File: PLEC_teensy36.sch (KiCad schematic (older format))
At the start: 4 parts, among them U8 Teensy3.6

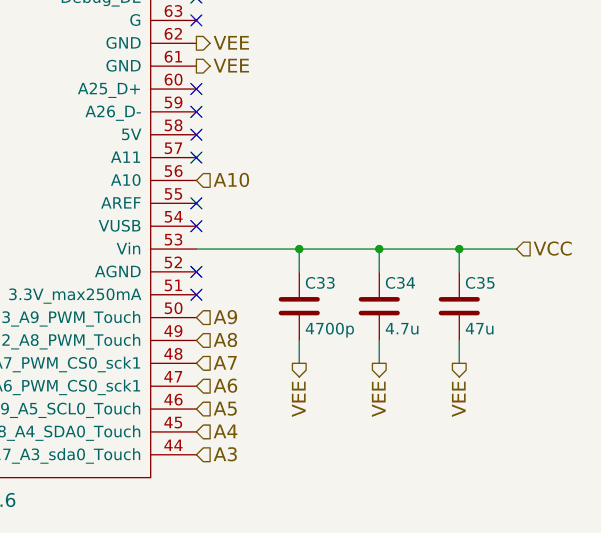
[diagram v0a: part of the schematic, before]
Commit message: Almost done with layout; need to rearrange uC pins
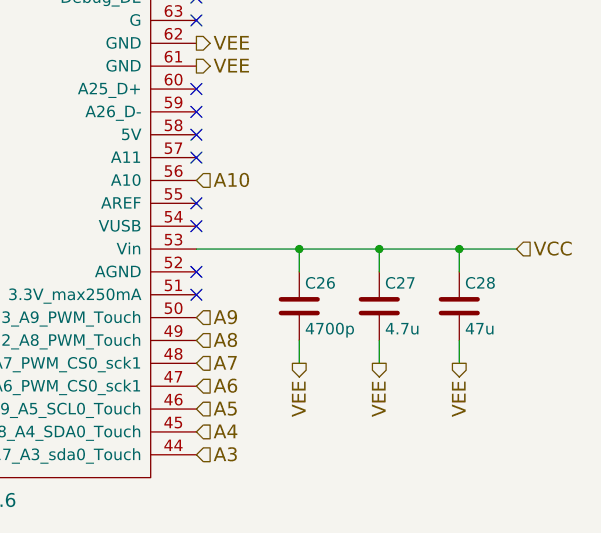
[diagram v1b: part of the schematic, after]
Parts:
- renumbered C33 to C26, C34 to C27, C35 to C28
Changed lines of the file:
@@
 NoConn ~ 6650 4600
 $Comp
-L C C34
+L C C27
 U 1 1 5A7ABA8B
 P 7450 5450
-F 0 "C34" H 7475 5550 50  0000 L CNN
+F 0 "C27" H 7475 5550 50  0000 L CNN
 F 1 "4.7u" H 7475 5350 50  0000 L CNN
 F 2 "PLEC:THTm_1.5Px4Dx7H_4.7u" H 7488 5300 50  0001 C CNN
@@
 $EndComp
 $Comp
-L C C33
+L C C26
 U 1 1 5A7ABABC
 P 7100 5450
-F 0 "C33" H 7125 5550 50  0000 L CNN
+F 0 "C26" H 7125 5550 50  0000 L CNN
 F 1 "4700p" H 7125 5350 50  0000 L CNN
 F 2 "PLEC:THTt_100Px150Lx100Wx183H_4700p" H 7138 5300 50  0001 C CNN
@@
 NoConn ~ 6650 5000
 $Comp
-L C C35
+L C C28
 U 1 1 5A75E6B2
 P 7800 5450
-F 0 "C35" H 7825 5550 50  0000 L CNN
+F 0 "C28" H 7825 5550 50  0000 L CNN
 F 1 "47u" H 7825 5350 50  0000 L CNN
 F 2 "PLEC:THTm_2Px4Dx12H_47u" H 7838 5300 50  0001 C CNN

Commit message: Finished PCB with no errors
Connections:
- net A0: now also U8.30 (33_A14_CAN1TX_scl0); no longer U8.41 (14_A0_PWM_sck0)
- net A1: now also U8.31 (34_A15_CAN1TX_sda0); no longer U8.42 (15_A1_CS0_Touch)
- net A10: now also U8.43 (16_A2_scl0_Touch); no longer U8.56 (A10)
- net A11: now also U8.44 (17_A3_sda0_Touch); no longer U8.38 (A22_DAC1)
- net A12: now also U8.41 (14_A0_PWM_sck0); no longer U8.79 (50_A24)
- net A13: now also U8.42 (15_A1_CS0_Touch); no longer U8.78 (49_A23)
- net A2: now also U8.32 (35_A16_PWM); no longer U8.43 (16_A2_scl0_Touch)
- net A3: now also U8.33 (36_A17_PWM); no longer U8.44 (17_A3_sda0_Touch)
- net A4: now also U8.34 (37_A18_PWM_SCL1); no longer U8.45 (18_A4_SDA0_Touch)
- net A5: now also U8.35 (38_A19_PWM_SDA1); no longer U8.46 (19_A5_SCL0_Touch)
- net A6: now also U8.36 (39_A20); no longer U8.47 (20_A6_PWM_CS0_sck1)
- net A7: now also U8.37 (A21_DAC0); no longer U8.48 (21_A7_PWM_CS0_sck1)
- net A8: now also U8.24 (32_A13_TX4_SCK1); no longer U8.49 (22_A8_PWM_Touch)
- net A9: now also U8.23 (31_A12_RX4_CS1); no longer U8.50 (23_A9_PWM_Touch)
- net D1: now also U8.45 (18_A4_SDA0_Touch); no longer U8.86 (57)
- net D2: now also U8.46 (19_A5_SCL0_Touch); no longer U8.85 (56)
- net D3: now also U8.47 (20_A6_PWM_CS0_sck1); no longer U8.84 (55)
- net D4: now also U8.49 (22_A8_PWM_Touch); no longer U8.83 (54_CS2)
- net D5: now also U8.50 (23_A9_PWM_Touch); no longer U8.82 (53_SCK2)
- net D6: now also U8.7 (5_PWM_tx1_miso1); no longer U8.71 (44_MOSI2)
- net D7: now also U8.8 (6_PWM); no longer U8.70 (43_CS2)
- net D8: now also U8.9 (7_RX3_miso0_scl0); no longer U8.69 (42)
- net D9: now also U8.10 (8_TX3_miso0_sda0); no longer U8.67 (40)
- net DAC0: now also U8.38 (A22_DAC1); no longer U8.37 (A21_DAC0)
- net DATA_~INTERRUPT: now also U8.11 (9_PWM_RX2_CS0); no longer U8.20 (28)
- net RF_~RESET: now also U8.22 (30_PWM_can0rx_Touch); no longer U8.18 (26_tx1)
- net RF_~SLEEP: now also U8.21 (29_PWM_can0tx_Touch); no longer U8.19 (27_rx1)
- net SPI_CLK: now also U8.19 (27_rx1); no longer U8.24 (32_A13_TX4_SCK1)
- net SPI_MISO: now also U8.14 (12_MISO0); no longer U8.3 (1_TX1_MISO1_Touch)
- net SPI_MOSI: now also U8.13 (11_MOSI0); no longer U8.2 (0_RX1_MOSI1_Touch)
- net SPI_SS: now also U8.48 (21_A7_PWM_CS0_sck1); no longer U8.23 (31_A12_RX4_CS1)
- net UART_RX: now also U8.2 (0_RX1_MOSI1_Touch); no longer U8.31 (34_A15_CAN1TX_sda0)
- net UART_TX: now also U8.3 (1_TX1_MISO1_Touch); no longer U8.30 (33_A14_CAN1TX_scl0)
- net UART_~CTS: now also U8.17 (25); no longer U8.16 (24)
- net UART_~RTS: now also U8.16 (24); no longer U8.17 (25)
- net VEE: no longer U8.27 (GND), U8.61 (GND), U8.62 (GND)
- no-connect marks 44 -> 47
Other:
- moved on the sheet: C26, C27, C28
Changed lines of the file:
@@
 Comment4 ""
 $EndDescr
-Text HLabel 8050 5200 2    60   Input ~ 0
+Text HLabel 8700 5200 2    60   Input ~ 0
 VCC
-Text HLabel 6650 4400 2    60   Output ~ 0
-VEE
+Text HLabel 4650 2000 0    60   Input ~ 0
+UART_RX
+Text HLabel 4650 2100 0    60   Output ~ 0
+UART_TX
+Text HLabel 4650 3500 0    60   Input ~ 0
+UART_~CTS
+Text HLabel 4650 3400 0    60   Output ~ 0
+UART_~RTS
+Text HLabel 4650 2900 0    60   Input ~ 0
+DATA_~INTERRUPT
+Text HLabel 4650 3700 0    60   Output ~ 0
+SPI_CLK
+Text HLabel 4650 3200 0    60   Input ~ 0
+SPI_MISO
+Text HLabel 4650 3100 0    60   Output ~ 0
+SPI_MOSI
+Text HLabel 6650 5700 2    60   Output ~ 0
+SPI_SS
+Text HLabel 4650 4000 0    60   Output ~ 0
+RF_~RESET
+Text HLabel 4650 3900 0    60   Output ~ 0
+RF_~SLEEP
+Text HLabel 4650 4800 0    60   Input ~ 0
+A0
 Text HLabel 4650 4900 0    60   Input ~ 0
-UART_RX
-Text HLabel 4650 4800 0    60   Output ~ 0
-UART_TX
-Text HLabel 4650 3400 0    60   Input ~ 0
-UART_~CTS
-Text HLabel 4650 3500 0    60   Output ~ 0
-UART_~RTS
-Text HLabel 4650 3800 0    60   Input ~ 0
-DATA_~INTERRUPT
-Text HLabel 4650 4200 0    60   Output ~ 0
-SPI_CLK
-Text HLabel 4650 2100 0    60   Input ~ 0
-SPI_MISO
-Text HLabel 4650 2000 0    60   Output ~ 0
-SPI_MOSI
-Text HLabel 4650 4100 0    60   Output ~ 0
-SPI_SS
-Text HLabel 4650 3600 0    60   Output ~ 0
-RF_~RESET
-Text HLabel 4650 3700 0    60   Output ~ 0
-RF_~SLEEP
+A1
+Text HLabel 4650 5000 0    60   Input ~ 0
+A2
+Text HLabel 4650 5100 0    60   Input ~ 0
+A3
+Text HLabel 4650 5200 0    60   Input ~ 0
+A4
+Text HLabel 4650 5300 0    60   Input ~ 0
+A5
+Text HLabel 4650 5400 0    60   Input ~ 0
+A6
+Text HLabel 4650 5500 0    60   Input ~ 0
+A7
+Text HLabel 4650 4200 0    60   Input ~ 0
+A8
+Text HLabel 4650 4100 0    60   Input ~ 0
+A9
+Text HLabel 4650 6100 0    60   Input ~ 0
+A10
+Text HLabel 6650 6100 2    60   Input ~ 0
+A11
 Text HLabel 4650 5900 0    60   Input ~ 0
-A0
+A12
 Text HLabel 4650 6000 0    60   Input ~ 0
-A1
-Text HLabel 4650 6100 0    60   Input ~ 0
-A2
-Text HLabel 6650 6100 2    60   Input ~ 0
-A3
-Text HLabel 6650 6000 2    60   Input ~ 0
-A4
-Text HLabel 6650 5900 2    60   Input ~ 0
-A5
-Text HLabel 6650 5800 2    60   Input ~ 0
-A6
-Text HLabel 6650 5700 2    60   Input ~ 0
-A7
-Text HLabel 6650 5600 2    60   Input ~ 0
-A8
-Text HLabel 6650 5500 2    60   Input ~ 0
-A9
-Text HLabel 6650 4900 2    60   Input ~ 0
-A10
-Text HLabel 4650 5600 0    60   Input ~ 0
-A11
-Text HLabel 6650 2600 2    60   Input ~ 0
-A12
-Text HLabel 6650 2700 2    60   Input ~ 0
 A13
 Text HLabel 4650 2300 0    60   Output ~ 0
 D0
-Text HLabel 6650 1900 2    60   Output ~ 0
+Text HLabel 6650 6000 2    60   Output ~ 0
 D1
-Text HLabel 6650 2000 2    60   Output ~ 0
+Text HLabel 6650 5900 2    60   Output ~ 0
 D2
-Text HLabel 6650 2100 2    60   Output ~ 0
+Text HLabel 6650 5800 2    60   Output ~ 0
 D3
-Text HLabel 6650 2200 2    60   Output ~ 0
+Text HLabel 6650 5600 2    60   Output ~ 0
 D4
-Text HLabel 6650 2300 2    60   Output ~ 0
+Text HLabel 6650 5500 2    60   Output ~ 0
 D5
-Text HLabel 6650 3400 2    60   Output ~ 0
+Text HLabel 4650 2500 0    60   Output ~ 0
 D6
-Text HLabel 6650 3500 2    60   Output ~ 0
+Text HLabel 4650 2600 0    60   Output ~ 0
 D7
-Text HLabel 6650 3600 2    60   Output ~ 0
+Text HLabel 4650 2700 0    60   Output ~ 0
 D8
-Text HLabel 6650 3800 2    60   Output ~ 0
+Text HLabel 4650 2800 0    60   Output ~ 0
 D9
-Text HLabel 4650 5500 0    60   Output ~ 0
+Text HLabel 4650 5600 0    60   Output ~ 0
 DAC0
-$Comp
-L Teensy3.6 U8
-U 1 1 5A7AA781
-P 5650 4000
-F 0 "U8" H 5650 6300 60  0000 C CNN
-F 1 "Teensy3.6" H 5650 1700 60  0000 C CNN
-F 2 "PLEC:teensy3.6" H 5650 4000 60  0001 C CNN
-F 3 "" H 5650 4000 60  0000 C CNN
-	1    5650 4000
-	1    0    0    -1
-$EndComp
 NoConn ~ 4650 3300
 NoConn ~ 4650 4400
 NoConn ~ 6650 5400
 NoConn ~ 6650 3000
-Text HLabel 6650 4300 2    60   Output ~ 0
-VEE
 Text HLabel 4650 1900 0    60   Output ~ 0
-VEE
-Text HLabel 4650 4500 0    60   Output ~ 0
 VEE
 Text HLabel 4650 5700 0    60   Output ~ 0
@@
 L C C27
 U 1 1 5A7ABA8B
-P 7450 5450
-F 0 "C27" H 7475 5550 50  0000 L CNN
-F 1 "4.7u" H 7475 5350 50  0000 L CNN
-F 2 "PLEC:THTm_1.5Px4Dx7H_4.7u" H 7488 5300 50  0001 C CNN
-F 3 "" H 7450 5450 50  0001 C CNN
-	1    7450 5450
+P 8100 5450
+F 0 "C27" H 8125 5550 50  0000 L CNN
+F 1 "4.7u" H 8125 5350 50  0000 L CNN
+F 2 "PLEC:THTm_1.5Px4Dx7H_4.7u" H 8138 5300 50  0001 C CNN
+F 3 "" H 8100 5450 50  0001 C CNN
+	1    8100 5450
 	1    0    0    -1
 $EndComp
@@
 L C C26
 U 1 1 5A7ABABC
-P 7100 5450
-F 0 "C26" H 7125 5550 50  0000 L CNN
-F 1 "4700p" H 7125 5350 50  0000 L CNN
-F 2 "PLEC:THTt_100Px150Lx100Wx183H_4700p" H 7138 5300 50  0001 C CNN
-F 3 "" H 7100 5450 50  0001 C CNN
-	1    7100 5450
+P 7750 5450
+F 0 "C26" H 7775 5550 50  0000 L CNN
+F 1 "4700p" H 7775 5350 50  0000 L CNN
+F 2 "PLEC:THTt_100Px150Lx100Wx183H_4700p" H 7788 5300 50  0001 C CNN
+F 3 "" H 7750 5450 50  0001 C CNN
+	1    7750 5450
 	1    0    0    -1
 $EndComp
 Wire Wire Line
-	6650 5200 8050 5200
+	6650 5200 8700 5200
 Wire Wire Line
-	7100 5300 7100 5200
-Connection ~ 7100 5200
+	7750 5300 7750 5200
+Connection ~ 7750 5200
 Wire Wire Line
-	7450 5300 7450 5200
-Connection ~ 7450 5200
+	8100 5300 8100 5200
+Connection ~ 8100 5200
 Wire Wire Line
-	7100 5600 7100 5700
+	7750 5600 7750 5700
 Wire Wire Line
-	7450 5600 7450 5700
-Text HLabel 7100 5700 3    60   Output ~ 0
+	8100 5600 8100 5700
+Text HLabel 7750 5700 3    60   Output ~ 0
 VEE
-Text HLabel 7450 5700 3    60   Output ~ 0
+Text HLabel 8100 5700 3    60   Output ~ 0
 VEE
 NoConn ~ 4650 2200
 NoConn ~ 4650 2400
-NoConn ~ 4650 2500
-NoConn ~ 4650 2600
-NoConn ~ 4650 2700
-NoConn ~ 4650 2800
-NoConn ~ 4650 2900
 NoConn ~ 4650 3000
-NoConn ~ 4650 3100
-NoConn ~ 4650 3200
-NoConn ~ 4650 3900
-NoConn ~ 4650 4000
 NoConn ~ 4650 4300
 NoConn ~ 4650 4600
-NoConn ~ 4650 5000
-NoConn ~ 4650 5100
-NoConn ~ 4650 5200
-NoConn ~ 4650 5300
-NoConn ~ 4650 5400
 NoConn ~ 4650 5800
 NoConn ~ 6650 5300
@@
 L C C28
 U 1 1 5A75E6B2
-P 7800 5450
-F 0 "C28" H 7825 5550 50  0000 L CNN
-F 1 "47u" H 7825 5350 50  0000 L CNN
-F 2 "PLEC:THTm_2Px4Dx12H_47u" H 7838 5300 50  0001 C CNN
-F 3 "" H 7800 5450 50  0001 C CNN
-	1    7800 5450
+P 8450 5450
+F 0 "C28" H 8475 5550 50  0000 L CNN
+F 1 "47u" H 8475 5350 50  0000 L CNN
+F 2 "PLEC:THTm_2Px4Dx12H_47u" H 8488 5300 50  0001 C CNN
+F 3 "" H 8450 5450 50  0001 C CNN
+	1    8450 5450
 	1    0    0    -1
 $EndComp
 Wire Wire Line
-	7800 5600 7800 5700
-Text HLabel 7800 5700 3    60   Output ~ 0
+	8450 5600 8450 5700
+Text HLabel 8450 5700 3    60   Output ~ 0
 VEE
 Wire Wire Line
-	7800 5300 7800 5200
-Connection ~ 7800 5200
+	8450 5300 8450 5200
+Connection ~ 8450 5200
+$Comp
+L Teensy3.6 U8
+U 1 1 5A7AA781
+P 5650 4000
+F 0 "U8" H 5650 6300 60  0000 C CNN
+F 1 "Teensy3.6" H 5650 1700 60  0000 C CNN
+F 2 "PLEC:teensy3.6" H 5650 4000 60  0001 C CNN
+F 3 "" H 5650 4000 60  0000 C CNN
+	1    5650 4000
+	1    0    0    -1
+$EndComp
+NoConn ~ 4650 4500
+NoConn ~ 4650 3800
+NoConn ~ 4650 3600
+NoConn ~ 6650 1900
+NoConn ~ 6650 2000
+NoConn ~ 6650 2100
+NoConn ~ 6650 2200
+NoConn ~ 6650 2300
+NoConn ~ 6650 2600
+NoConn ~ 6650 2700
+NoConn ~ 6650 3400
+NoConn ~ 6650 3500
+NoConn ~ 6650 3600
+NoConn ~ 6650 3800
+NoConn ~ 6650 4300
+NoConn ~ 6650 4400
+NoConn ~ 6650 4900
 $EndSCHEMATC

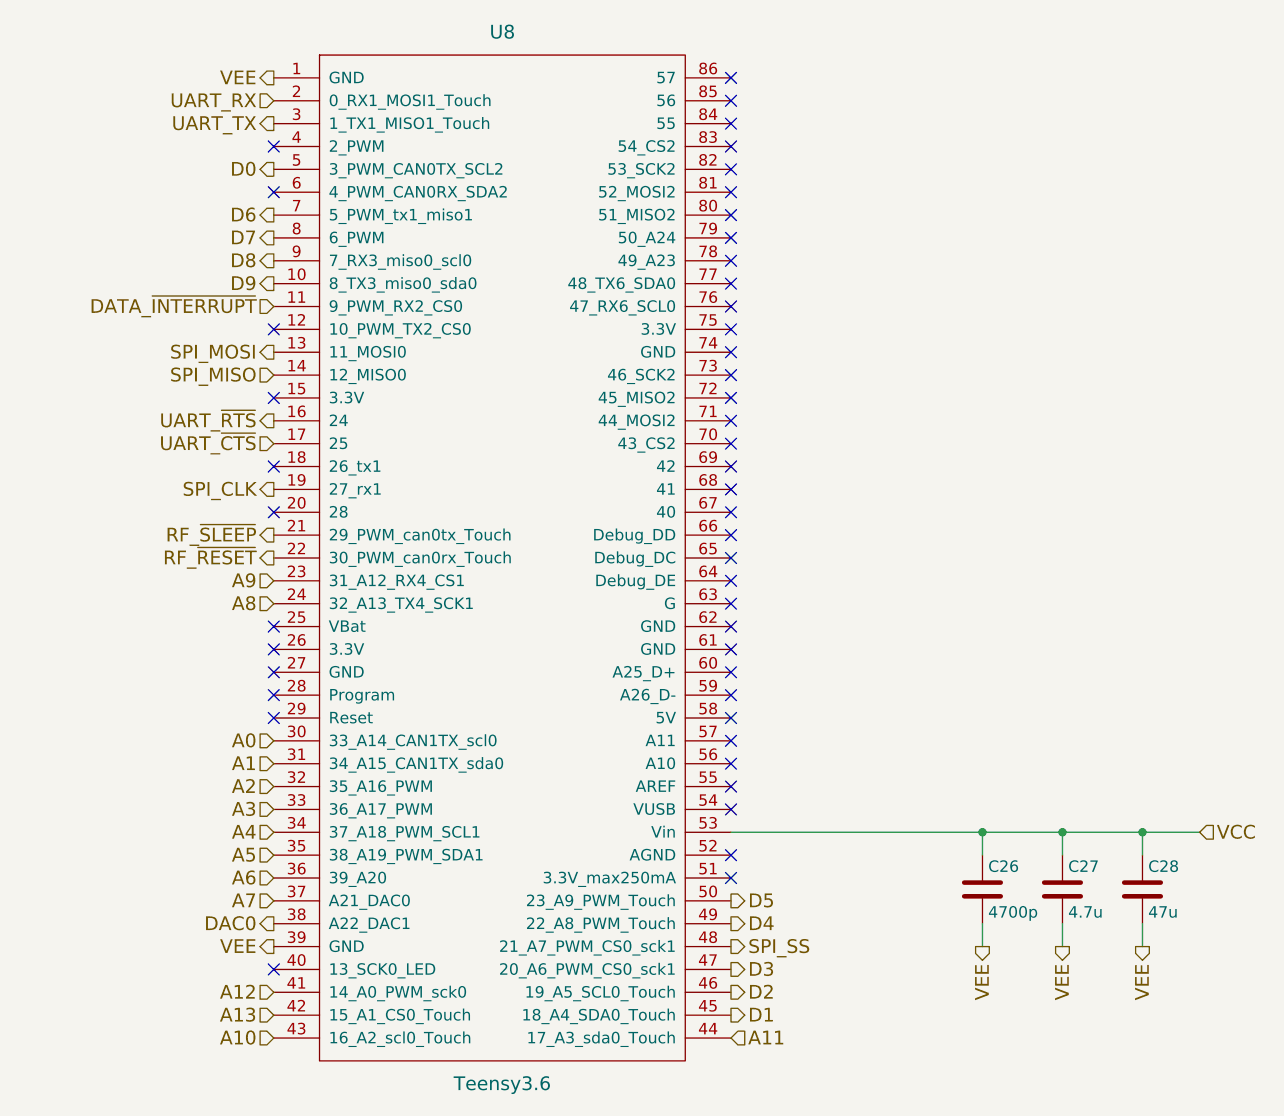
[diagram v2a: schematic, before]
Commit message: Replaced solid state relays with NPN Darlingtons
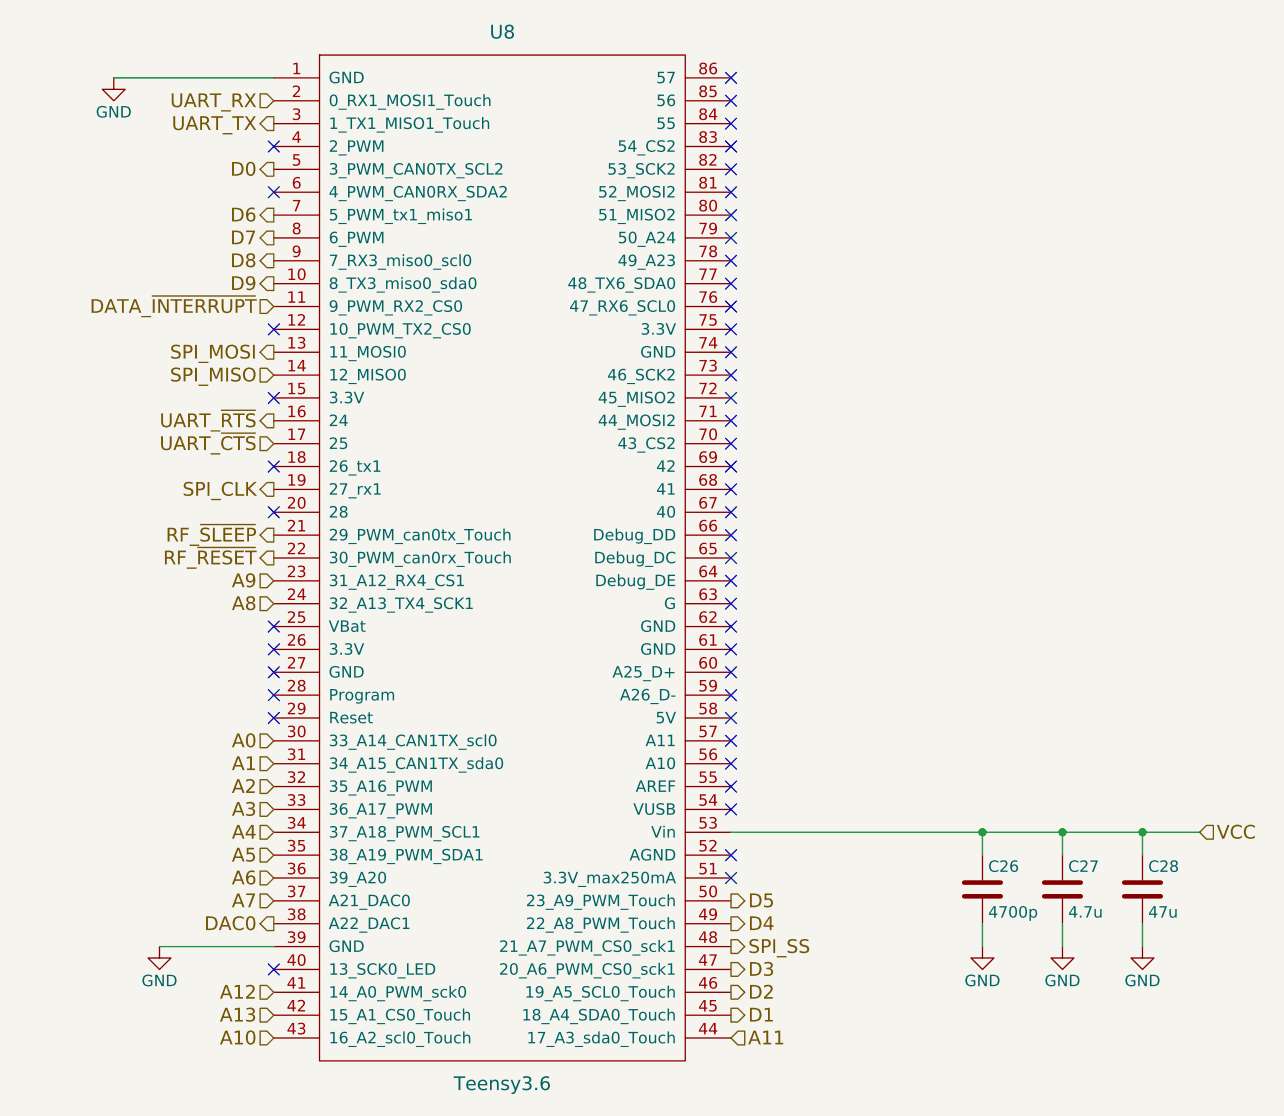
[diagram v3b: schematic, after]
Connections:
- net VEE renamed GND
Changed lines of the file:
@@
 EESchema Schematic File Version 2
+LIBS:PLEC-rescue
 LIBS:power
 LIBS:device
@@
 LIBS:PLEC
 LIBS:cap_470u
+LIBS:BDW42G
 LIBS:PLEC-cache
 EELAYER 25 0
@@
 $Descr A4 11693 8268
 encoding utf-8
-Sheet 9 9
+Sheet 8 9
 Title ""
 Date ""
@@
 NoConn ~ 6650 5400
 NoConn ~ 6650 3000
-Text HLabel 4650 1900 0    60   Output ~ 0
-VEE
-Text HLabel 4650 5700 0    60   Output ~ 0
-VEE
 NoConn ~ 4650 4700
 NoConn ~ 6650 4700
@@
 Wire Wire Line
 	8100 5600 8100 5700
-Text HLabel 7750 5700 3    60   Output ~ 0
-VEE
-Text HLabel 8100 5700 3    60   Output ~ 0
-VEE
 NoConn ~ 4650 2200
 NoConn ~ 4650 2400
@@
 Wire Wire Line
 	8450 5600 8450 5700
-Text HLabel 8450 5700 3    60   Output ~ 0
-VEE
 Wire Wire Line
 	8450 5300 8450 5200
@@
 NoConn ~ 6650 4400
 NoConn ~ 6650 4900
+$Comp
+L GND #PWR035
+U 1 1 5A84EF25
+P 7750 5700
+F 0 "#PWR035" H 7750 5450 50  0001 C CNN
+F 1 "GND" H 7750 5550 50  0000 C CNN
+F 2 "" H 7750 5700 50  0001 C CNN
+F 3 "" H 7750 5700 50  0001 C CNN
+	1    7750 5700
+	1    0    0    -1
+$EndComp
+$Comp
+L GND #PWR036
+U 1 1 5A84EF7A
+P 8100 5700
+F 0 "#PWR036" H 8100 5450 50  0001 C CNN
+F 1 "GND" H 8100 5550 50  0000 C CNN
+F 2 "" H 8100 5700 50  0001 C CNN
+F 3 "" H 8100 5700 50  0001 C CNN
+	1    8100 5700
+	1    0    0    -1
+$EndComp
+$Comp
+L GND #PWR037
+U 1 1 5A84EF91
+P 8450 5700
+F 0 "#PWR037" H 8450 5450 50  0001 C CNN
+F 1 "GND" H 8450 5550 50  0000 C CNN
+F 2 "" H 8450 5700 50  0001 C CNN
+F 3 "" H 8450 5700 50  0001 C CNN
+	1    8450 5700
+	1    0    0    -1
+$EndComp
+$Comp
+L GND #PWR038
+U 1 1 5A84F2D1
+P 4150 5700
+F 0 "#PWR038" H 4150 5450 50  0001 C CNN
+F 1 "GND" H 4150 5550 50  0000 C CNN
+F 2 "" H 4150 5700 50  0001 C CNN
+F 3 "" H 4150 5700 50  0001 C CNN
+	1    4150 5700
+	1    0    0    -1
+$EndComp
+Wire Wire Line
+	4150 5700 4650 5700
+$Comp
+L GND #PWR039
+U 1 1 5A84F67A
+P 3950 1900
+F 0 "#PWR039" H 3950 1650 50  0001 C CNN
+F 1 "GND" H 3950 1750 50  0000 C CNN
+F 2 "" H 3950 1900 50  0001 C CNN
+F 3 "" H 3950 1900 50  0001 C CNN
+	1    3950 1900
+	1    0    0    -1
+$EndComp
+Wire Wire Line
+	3950 1900 4650 1900
 $EndSCHEMATC
